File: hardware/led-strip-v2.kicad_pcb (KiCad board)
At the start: 2 copper layers, 30 x 30 mm, 42 parts, among them J1 AKL_5_2, J2 AKL_5_2, J3 AKL_5_2, P1 CON-SENSOR, P2 TST, P3 TST, P4 TST, P5 TST, P6 TST, P7 TST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

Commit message: version 2.1, improve ground connection
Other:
- board text added: "LED Strip 2.1"
- board text removed: "LED Strip 2.0"

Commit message: specify fuse
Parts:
- F1: value FUSE -> 0ZCJ0035FF2G

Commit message: add 2.2 data
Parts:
- removed F1: 0ZCJ0035FF2G, kicad-libraries:F1206
- removed the G*** at (61.5, 28.3)
- removed Q1, Q2: 2N7002P, kicad-libraries:SOT23GDS
- removed RP3: 1k, kicad-libraries:4X0603
- added C5: 100nF, kicad-libraries:C0603F, F.Cu at (56.4, 45.2)
- added C6: DNP, kicad-libraries:C0603F, F.Cu at (58.9, 45.8)
- added C7: DNP, kicad-libraries:C0603F, F.Cu at (58.9, 52.2)
- added C8: 100nF, kicad-libraries:C0603F, F.Cu at (50.0, 40.9)
- added C9: 100nF, kicad-libraries:C0603F, F.Cu at (53.9, 40.9)
- added Fiducial_Mark: VAL**, kicad-libraries:Fiducial_Mark, F.Cu at (65.4, 29.8)
- added L2: FB, kicad-libraries:R0603F, F.Cu at (52.0, 40.1)
- added R6: 100, kicad-libraries:R0603F, F.Cu at (58.9, 42.9)
- added R7: 100, kicad-libraries:R0603F, F.Cu at (58.9, 49.2)
- added U6: 74LVC1G17, kicad-libraries:SOT23-5, F.Cu at (56.4, 43.0)
- added U7: 74LVC1G17, kicad-libraries:SOT23-5, F.Cu at (56.4, 47.5)
- L1: value FB -> 0
- moved Fiducial_Mark 24.4 mm to (44.4, 39.3)
- moved Fiducial_Mark 21.6 mm to (65.9, 55.3)
- moved C2 10.3 mm to (45.7, 50.0), turned to 180 degrees
- moved C4 5.37 mm to (56.4, 40.7)
- moved D1 1.89 mm to (60.3, 43.7), turned to 90 degrees
- moved R1 1.46 mm to (52.1, 44.4)
- moved R2 1.46 mm to (52.1, 43.0)
- moved R5 1.05 mm to (56.3, 50.5)
- moved D2 1.02 mm to (60.3, 50.1), turned to 90 degrees
- moved P8 0.62 mm to (57.1, 52.8)
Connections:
- C4 pad 2: GND -> AGND
- D1 pad 2: Net-(D1-Pad2) -> AGND
- D2 pad 2: Net-(D1-Pad2) -> AGND
- P1 pad 1: +5V -> Net-(C8-Pad1)
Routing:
- net Net-(D1-Pad2): track 38.0 -> 0.00 mm, vias 9 -> 0
- net Net-(J1-Pad2): track 28.1 -> 57.2 mm, vias 1 -> 0
- net AGND: track 16.1 -> 26.5 mm, vias 0 -> 16
- net Net-(C8-Pad1): track 0.00 -> 4.79 mm
- net Net-(C6-Pad1): track 17.4 -> 13.4 mm
- net Net-(C7-Pad1): track 17.5 -> 14.1 mm
- net GND: track 22.0 -> 24.7 mm, vias 12 -> 15
- net Net-(R4-Pad2): track 7.02 -> 4.39 mm, vias 2 -> 0
- net VCC: track 37.1 -> 34.5 mm, vias 2 -> 0
- net Net-(R6-Pad1): track 0.00 -> 2.48 mm
- net Net-(R7-Pad1): track 0.00 -> 1.42 mm
- net +5V: track 17.3 -> 16.0 mm, vias 0 -> 2
- net Net-(R5-Pad2): track 3.11 -> 3.48 mm, vias 2 -> 0
- added copper zone on B.Cu, net AGND
- removed copper zone on F.Cu, net AGND
- removed copper zone on B.Cu, net Net-(D1-Pad2)
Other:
- board text added: "LED Strip 2.2"
- board text removed: "LED Strip 2.1"

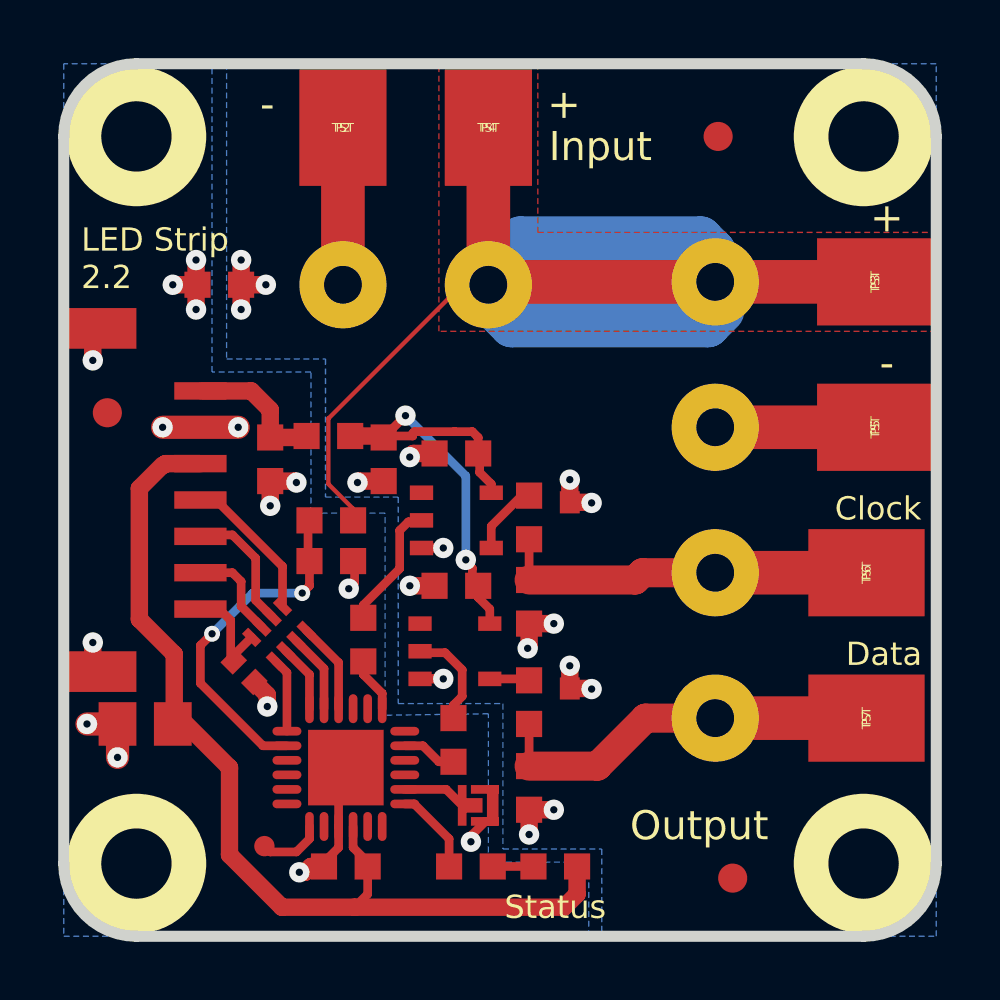
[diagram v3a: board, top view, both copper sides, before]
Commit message: add version detection pin to pcb
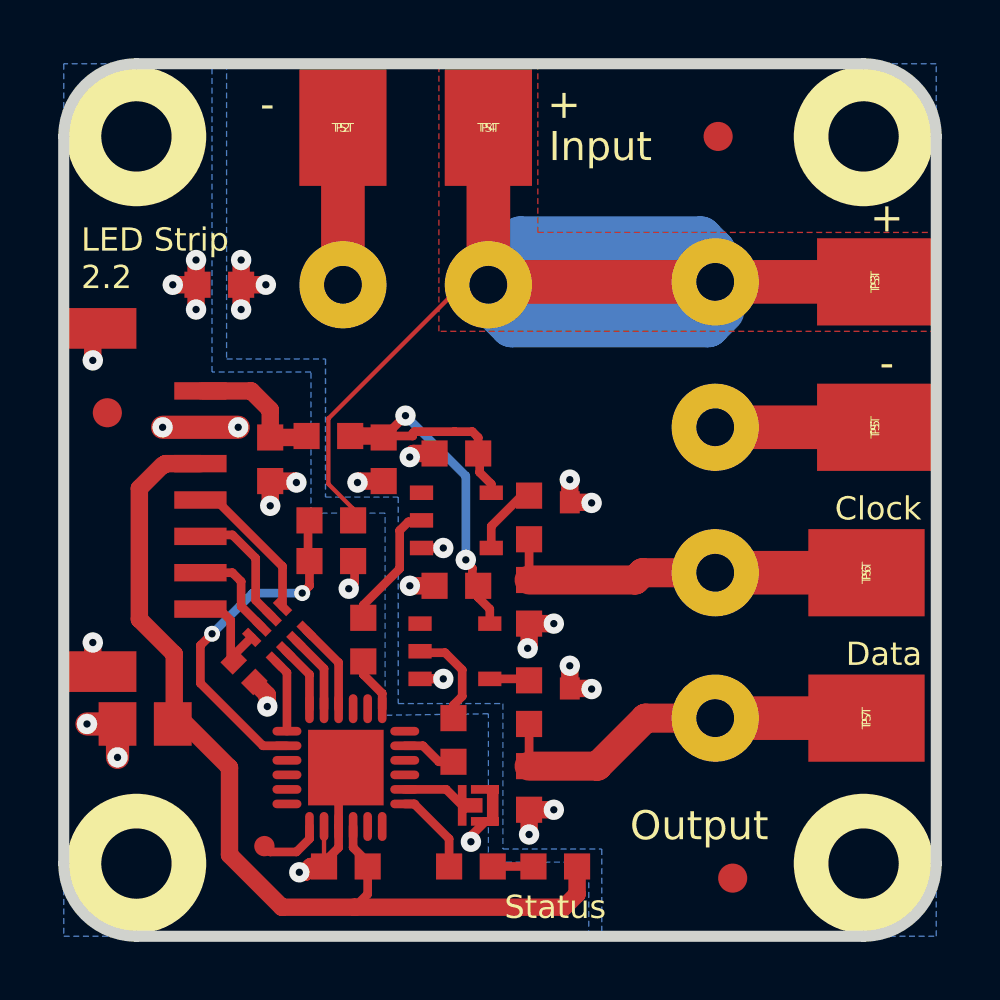
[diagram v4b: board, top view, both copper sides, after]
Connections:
- U1 pad 11: Net-(U1-Pad11) -> unconnected-(U1-Pad11)
- U1 pad 12: Net-(U1-Pad12) -> unconnected-(U1-Pad12)
- U1 pad 15: Net-(U1-Pad15) -> unconnected-(U1-Pad15)
- U1 pad 16: Net-(U1-Pad16) -> unconnected-(U1-Pad16)
- U1 pad 18: Net-(U1-Pad18) -> unconnected-(U1-Pad18)
- U1 pad 20: Net-(U1-Pad20) -> unconnected-(U1-Pad20)
- U1 pad 21: Net-(U1-Pad21) -> unconnected-(U1-Pad21)
- U1 pad 3: Net-(U1-Pad3) -> unconnected-(U1-Pad3)
- U1 pad 4: Net-(U1-Pad4) -> unconnected-(U1-Pad4)
- U1 pad 5: Net-(U1-Pad5) -> unconnected-(U1-Pad5)
- U1 pad 6: Net-(U1-Pad6) -> unconnected-(U1-Pad6)
- U1 pad 8: Net-(U1-Pad8) -> GND
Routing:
- net GND: track 24.7 -> 26.0 mm
- net AGND: track 26.5 -> 25.9 mm
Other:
- net class Default removed

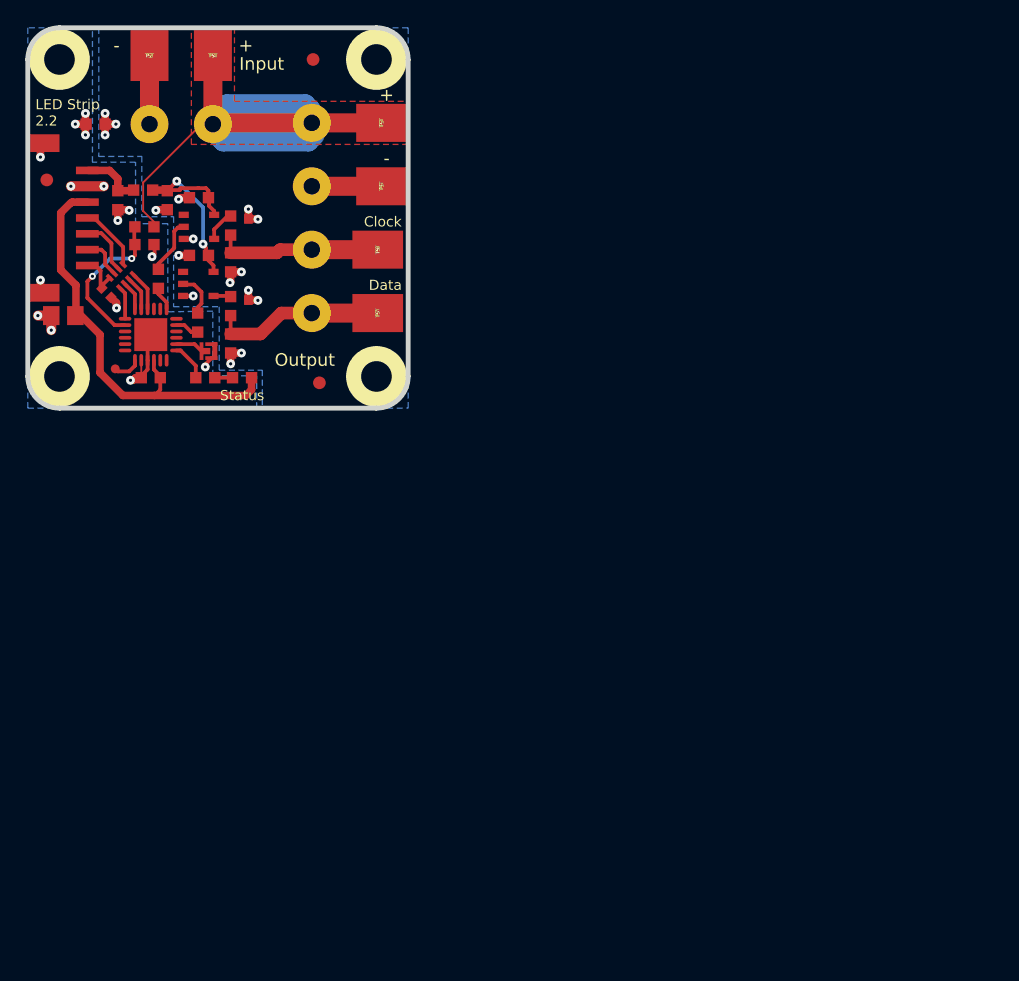
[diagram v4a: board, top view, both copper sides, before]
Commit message: New standart layout. Switched to Kicad 6
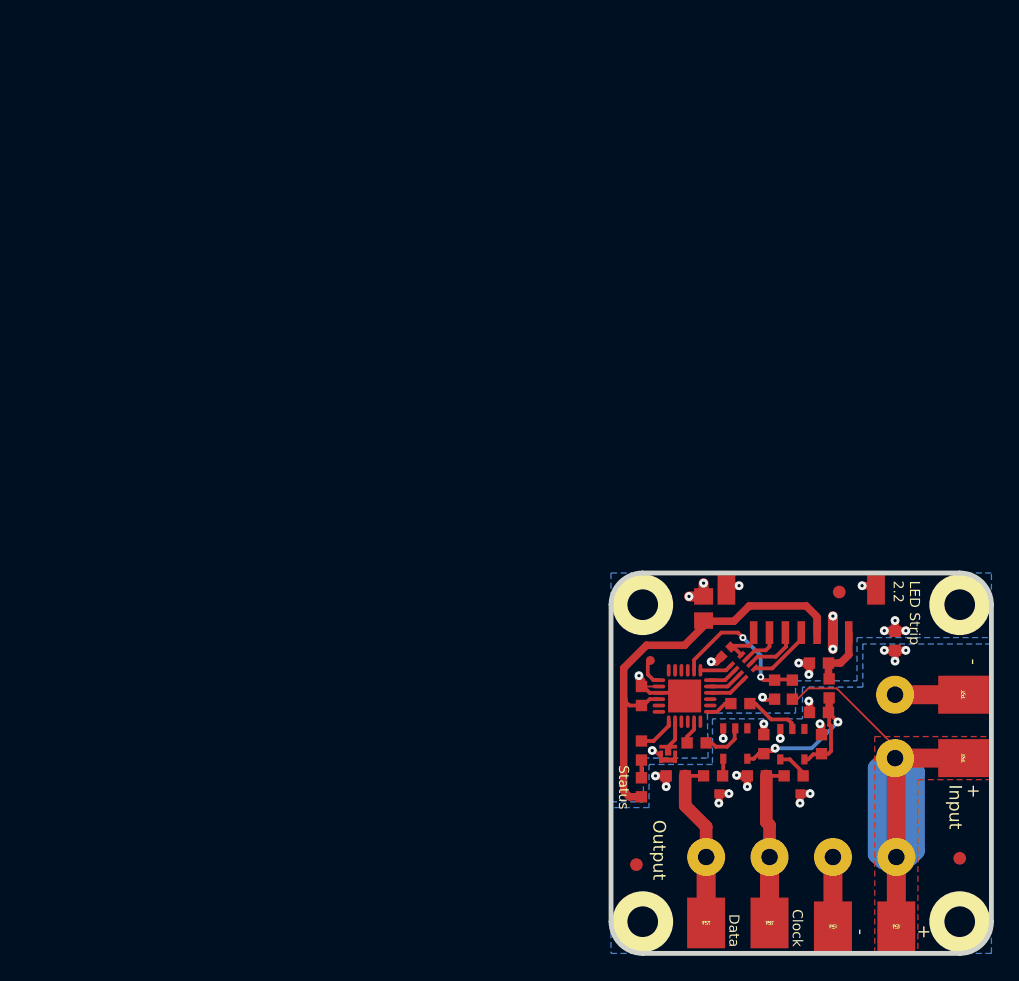
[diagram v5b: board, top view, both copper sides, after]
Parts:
- moved U5 83.0 mm to (116.4, 72.8), turned to -90 degrees
- moved U3 82.1 mm to (116.4, 97.8), turned to -90 degrees
- moved P2 81.6 mm to (116.7, 79.9), turned to 90 degrees
- moved P4 81.1 mm to (116.7, 84.9), turned to -90 degrees
- moved Fiducial_Mark 81.1 mm to (116.4, 92.8), turned to -90 degrees
- moved G*** 79.9 mm to (115.9, 85.3), turned to -90 degrees
- moved P3 75.3 mm to (111.4, 98.2), turned to 0 degrees
- moved L1 75.1 mm to (111.3, 75.7), turned to -90 degrees
- moved J1 73.7 mm to (111.3, 82.4), turned to -90 degrees
- moved J2 70.5 mm to (108.9, 92.7), turned to 180 degrees
- moved Fiducial_Mark 70.4 mm to (106.9, 71.8), turned to -90 degrees
- moved P5 68.4 mm to (106.4, 98.2), turned to 0 degrees
- moved VAL 67.2 mm to (106.9, 85.3), turned to -90 degrees
- moved P1 67.1 mm to (103.9, 70.4), turned to 180 degrees
- moved L2 66.9 mm to (106.1, 79.4), turned to -90 degrees
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
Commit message: Data Cleanup
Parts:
- G***: value Logo_31x31 -> LOGO
- moved G*** 15.5 mm to (104.0, 75.4)
- moved G*** 2.06 mm to (91.3, 85.3)
- moved P3 0.30 mm to (111.4, 97.9)
- moved P5 0.30 mm to (106.4, 97.9)
- moved L1 0.05 mm to (111.3, 75.6)
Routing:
- net Net-(P8-Pad2): track 3.15 -> 2.60 mm
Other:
- board text added: "Copyright Tinkerforge GmbH 2023. This documentation describes Open Hardware and is licensed under the CERN OHL v. 1.1. You may redistribute and modify this documentation under the terms of the CERN OHL v.1.1. (http://ohwr.org/cernohl). This documentation is distributed WITHOUT ANY EXPRESS OR IMPLIED WARRANTY, INCLUDING OF MERCHANTABILITY, SATISFACTORY QUALITY AND FITNESS FOR A PARTICULAR PURPOSE.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"
- board text removed: "Copyright Tinkerforge GmbH 2013. This documentation describes Open Hardware and is licensed under the CERN OHL v. 1.1. You may redistribute and modify this documentation under the terms of the CERN OHL v.1.1. (http://ohwr.org/cernohl). This documentation is distributed WITHOUT ANY EXPRESS OR IMPLIED WARRANTY, INCLUDING OF MERCHANTABILITY, SATISFACTORY QUALITY AND FITNESS FOR A PARTICULAR PURPOSE.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"
